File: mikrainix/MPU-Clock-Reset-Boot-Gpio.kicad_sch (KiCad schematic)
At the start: 17 parts, among them SW3 BPOR, SW4 BBOOT, U7 RV1106G3, Y2 32.768KHz, Y3 24MHz

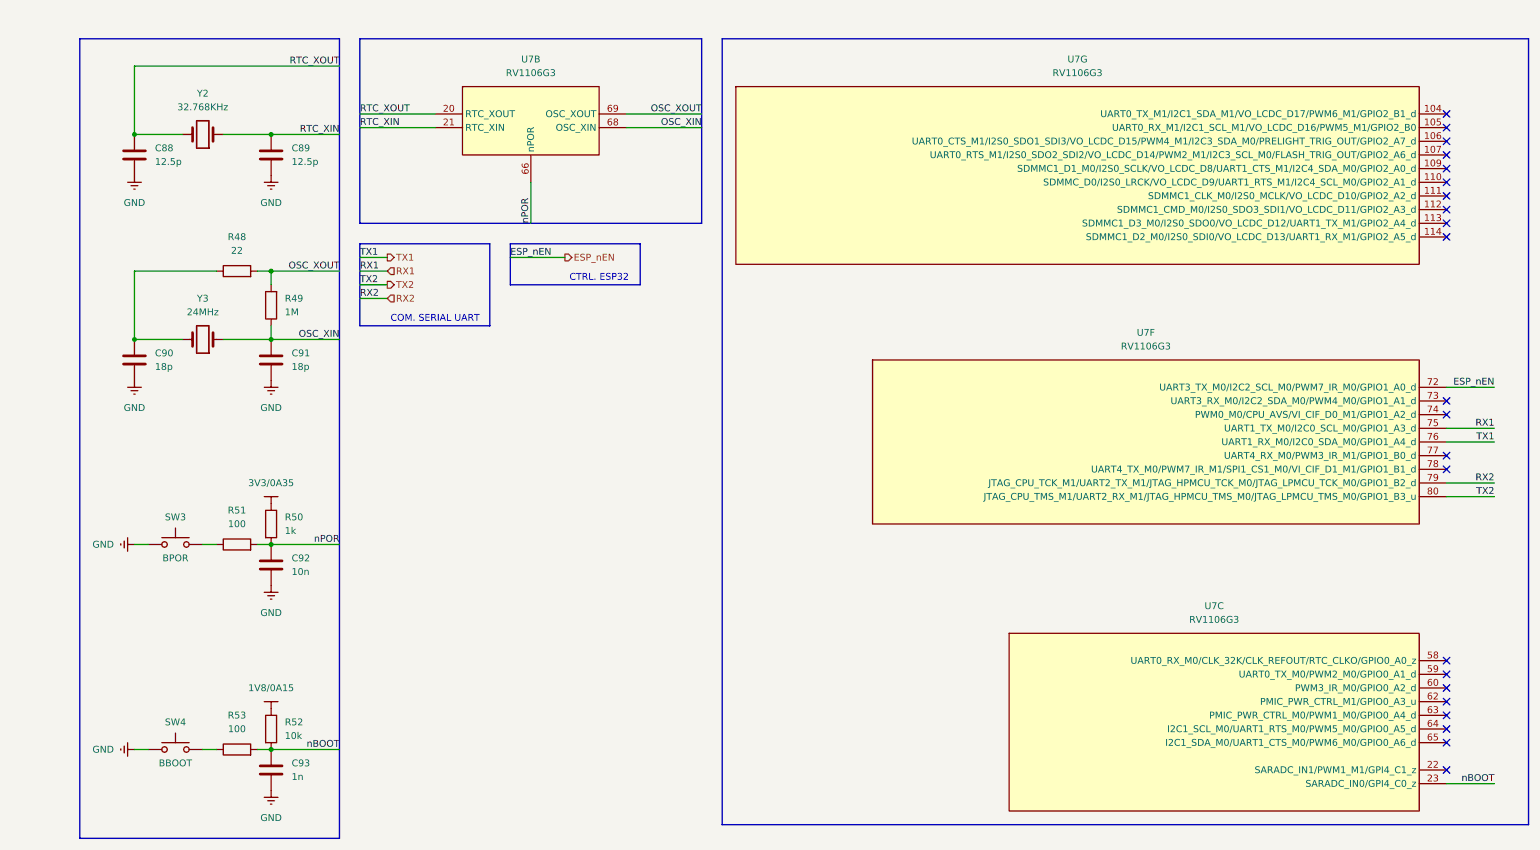
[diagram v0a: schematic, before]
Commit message: add MIS5001 camera and Ethernet, replace ESP32-C6-MINI > ESP32-MINI-1
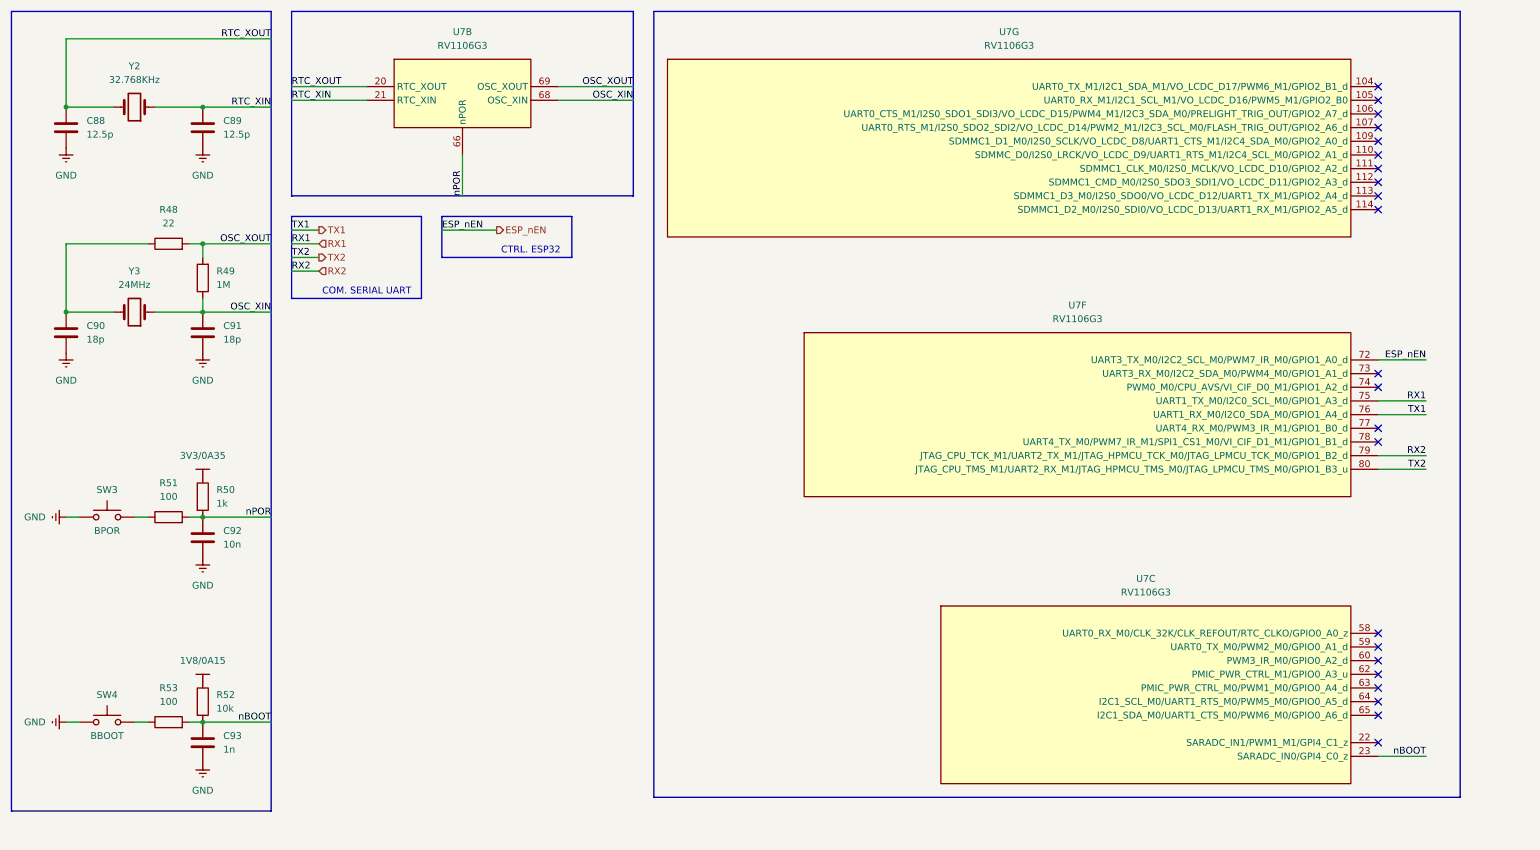
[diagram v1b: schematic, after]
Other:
- title: MPU – Clock, Reset, Boot & GPIO -> MPU–Clock, Reset, Boot & GPIO
- moved on the sheet: C88, C89, C90, C91, C92, C93, R48, R49, R50, R51, R52, R53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

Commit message: add microSD and resolve ERC issues
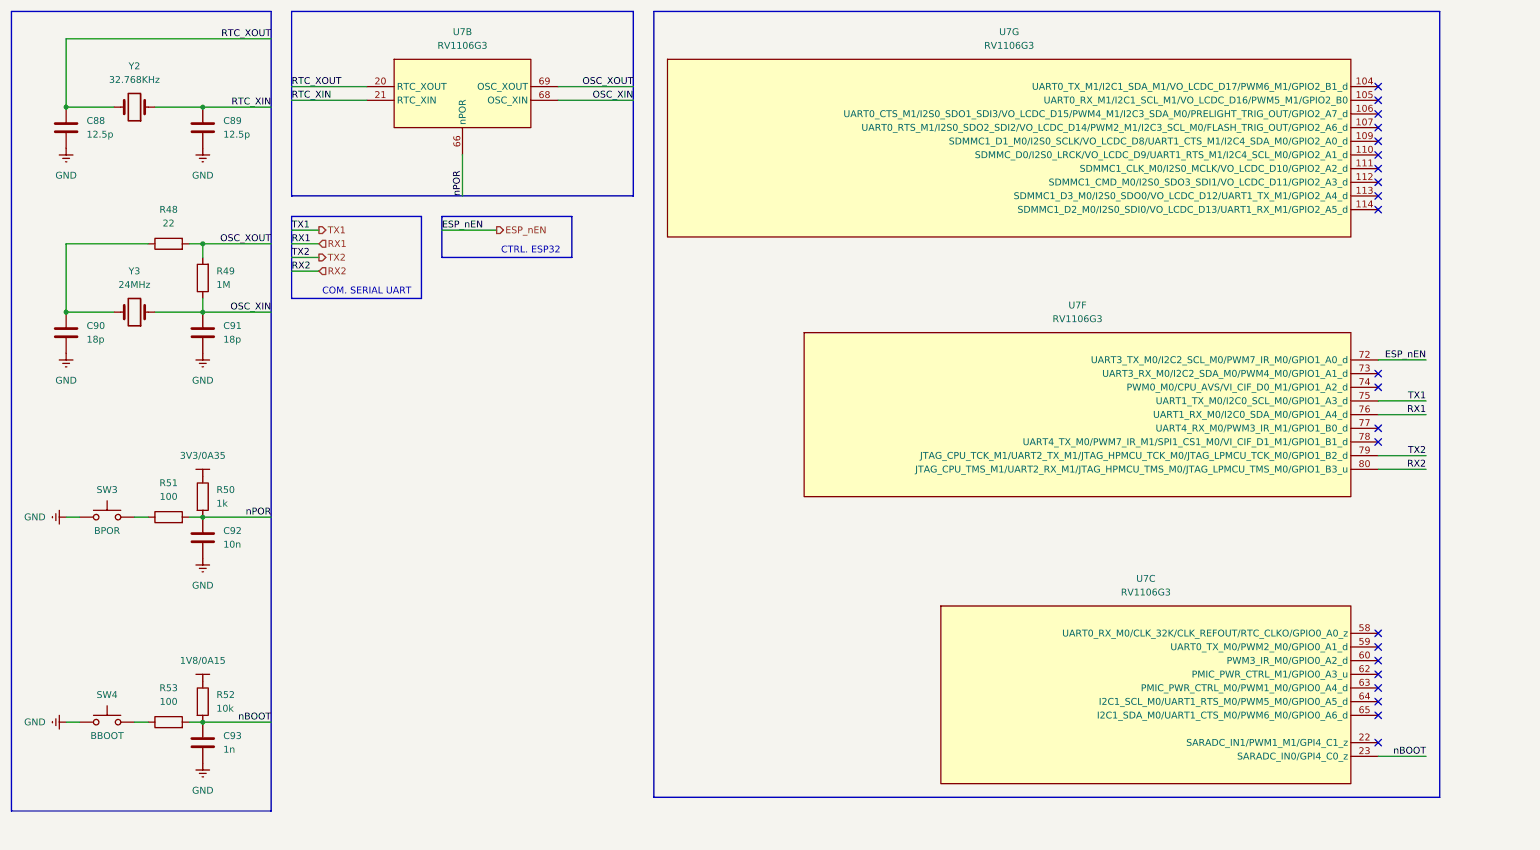
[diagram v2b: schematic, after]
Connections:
- net RX1: now also U7.76 (UART1_RX_M0/I2C0_SDA_M0/GPIO1_A4_d); no longer U7.75 (UART1_TX_M0/I2C0_SCL_M0/GPIO1_A3_d)
- net RX2: now also U7.80 (JTAG_CPU_TMS_M1/UART2_RX_M1/JTAG_HPMCU_TMS_M0/JTAG_LPMCU_TMS_M0/GPIO1_B3_u); no longer U7.79 (JTAG_CPU_TCK_M1/UART2_TX_M1/JTAG_HPMCU_TCK_M0/JTAG_LPMCU_TCK_M0/GPIO1_B2_d)
- net TX1: now also U7.75 (UART1_TX_M0/I2C0_SCL_M0/GPIO1_A3_d); no longer U7.76 (UART1_RX_M0/I2C0_SDA_M0/GPIO1_A4_d)
- net TX2: now also U7.79 (JTAG_CPU_TCK_M1/UART2_TX_M1/JTAG_HPMCU_TCK_M0/JTAG_LPMCU_TCK_M0/GPIO1_B2_d); no longer U7.80 (JTAG_CPU_TMS_M1/UART2_RX_M1/JTAG_HPMCU_TMS_M0/JTAG_LPMCU_TMS_M0/GPIO1_B3_u)
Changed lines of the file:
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@@
 	(title_block
 		(title "MPU–Clock, Reset, Boot & GPIO")
-		(date "2026-10-14")
+		(date "2026-10-21")
+		(rev "v0.1")
 		(comment 1 "Project repository: github.com/ndkimdavy/Mikrainix")
 		(comment 2 "Designed by: Kim Davy NDAYONGEJE")
@@
 	(rectangle
 		(start 134.62 15.24)
-		(end 284.48 161.29)
+		(end 280.67 161.29)
 		(stroke
 			(width 0.254)
@@
 	(wire
 		(pts
-			(xy 48.26 147.32) (xy 50.8 147.32)
+			(xy 269.24 100.33) (xy 278.13 100.33)
 		)
 		(stroke
@@
 	(wire
 		(pts
-			(xy 50.8 109.22) (xy 63.5 109.22)
+			(xy 48.26 147.32) (xy 50.8 147.32)
 		)
 		(stroke
@@
 	(wire
 		(pts
-			(xy 269.24 90.17) (xy 278.13 90.17)
+			(xy 50.8 109.22) (xy 63.5 109.22)
 		)
 		(stroke
@@
 	(wire
 		(pts
-			(xy 269.24 97.79) (xy 278.13 97.79)
+			(xy 72.39 55.88) (xy 67.31 55.88)
 		)
 		(stroke
@@
 	(wire
 		(pts
-			(xy 72.39 58.42) (xy 67.31 58.42)
+			(xy 25.4 71.12) (xy 34.29 71.12)
 		)
 		(stroke
@@
 	(wire
 		(pts
-			(xy 25.4 71.12) (xy 34.29 71.12)
+			(xy 269.24 97.79) (xy 278.13 97.79)
 		)
 		(stroke
@@
 	(wire
 		(pts
-			(xy 38.1 109.22) (xy 40.64 109.22)
+			(xy 269.24 87.63) (xy 278.13 87.63)
 		)
 		(stroke
@@
 	(wire
 		(pts
-			(xy 25.4 58.42) (xy 40.64 58.42)
+			(xy 38.1 109.22) (xy 40.64 109.22)
 		)
 		(stroke
@@
 	(wire
 		(pts
-			(xy 48.26 58.42) (xy 50.8 58.42)
+			(xy 25.4 58.42) (xy 40.64 58.42)
 		)
 		(stroke
@@
 	(wire
 		(pts
-			(xy 63.5 20.32) (xy 25.4 20.32)
+			(xy 269.24 90.17) (xy 278.13 90.17)
 		)
 		(stroke
@@
 	(wire
 		(pts
-			(xy 72.39 63.5) (xy 67.31 63.5)
+			(xy 72.39 58.42) (xy 67.31 58.42)
 		)
 		(stroke
@@
 	(wire
 		(pts
-			(xy 50.8 58.42) (xy 50.8 60.96)
+			(xy 48.26 58.42) (xy 50.8 58.42)
 		)
 		(stroke
@@
 	(wire
 		(pts
-			(xy 105.41 55.88) (xy 95.25 55.88)
+			(xy 63.5 20.32) (xy 25.4 20.32)
 		)
 		(stroke
@@
 	(wire
 		(pts
-			(xy 25.4 58.42) (xy 25.4 71.12)
+			(xy 50.8 58.42) (xy 50.8 60.96)
 		)
 		(stroke
@@
 	(wire
 		(pts
-			(xy 72.39 55.88) (xy 67.31 55.88)
+			(xy 105.41 55.88) (xy 95.25 55.88)
 		)
 		(stroke
@@
 	(wire
 		(pts
-			(xy 269.24 80.01) (xy 278.13 80.01)
+			(xy 25.4 58.42) (xy 25.4 71.12)
 		)
 		(stroke
@@
 	(wire
 		(pts
-			(xy 269.24 153.67) (xy 278.13 153.67)
+			(xy 72.39 63.5) (xy 67.31 63.5)
 		)
 		(stroke
@@
 	(wire
 		(pts
-			(xy 116.84 31.75) (xy 130.81 31.75)
+			(xy 269.24 80.01) (xy 278.13 80.01)
 		)
 		(stroke
@@
 	(wire
 		(pts
-			(xy 67.31 31.75) (xy 81.28 31.75)
+			(xy 269.24 153.67) (xy 278.13 153.67)
 		)
 		(stroke
@@
 	(wire
 		(pts
-			(xy 269.24 100.33) (xy 278.13 100.33)
+			(xy 116.84 31.75) (xy 130.81 31.75)
 		)
 		(stroke
@@
 	(wire
 		(pts
-			(xy 99.06 41.91) (xy 99.06 49.53)
+			(xy 67.31 31.75) (xy 81.28 31.75)
 		)
 		(stroke
@@
 	(wire
 		(pts
-			(xy 50.8 33.02) (xy 63.5 33.02)
+			(xy 99.06 41.91) (xy 99.06 49.53)
 		)
 		(stroke
@@
 	(wire
 		(pts
-			(xy 50.8 71.12) (xy 63.5 71.12)
+			(xy 50.8 33.02) (xy 63.5 33.02)
 		)
 		(stroke
@@
 	(wire
 		(pts
-			(xy 269.24 87.63) (xy 278.13 87.63)
+			(xy 50.8 71.12) (xy 63.5 71.12)
 		)
 		(stroke
@@
 		)
 	)
-	(label "nPOR"
-		(at 99.06 49.53 90)
+	(label "TX2"
+		(at 67.31 60.96 0)
 		(effects
 			(font
@@
 		)
 	)
-	(label "nBOOT"
-		(at 278.13 153.67 180)
+	(label "nPOR"
+		(at 99.06 49.53 90)
 		(effects
 			(font
 				(size 1.27 1.27)
 			)
-			(justify right bottom)
+			(justify left bottom)
 		)
 	)
-	(label "TX2"
-		(at 67.31 60.96 0)
+	(label "nBOOT"
+		(at 278.13 153.67 180)
 		(effects
 			(font
 				(size 1.27 1.27)
 			)
-			(justify left bottom)
+			(justify right bottom)
 		)
 	)
 	(label "RX2"
-		(at 278.13 97.79 180)
+		(at 278.13 100.33 180)
 		(effects
 			(font
@@
 		)
 	)
-	(label "RX2"
-		(at 67.31 63.5 0)
-		(effects
-			(font
-				(size 1.27 1.27)
-			)
-			(justify left bottom)
-		)
-	)
 	(label "TX1"
-		(at 278.13 90.17 180)
+		(at 278.13 87.63 180)
 		(effects
 			(font
@@
 	)
 	(label "TX2"
-		(at 278.13 100.33 180)
+		(at 278.13 97.79 180)
 		(effects
 			(font
@@
 		)
 	)
+	(label "TX1"
+		(at 67.31 55.88 0)
+		(effects
+			(font
+				(size 1.27 1.27)
+			)
+			(justify left bottom)
+		)
+	)
 	(label "nPOR"
 		(at 63.5 109.22 180)
@@
 	)
 	(label "RX1"
-		(at 278.13 87.63 180)
+		(at 278.13 90.17 180)
 		(effects
 			(font
@@
 		)
 	)
-	(label "TX1"
-		(at 67.31 55.88 0)
+	(label "RTC_XIN"
+		(at 63.5 33.02 180)
 		(effects
 			(font
 				(size 1.27 1.27)
 			)
-			(justify left bottom)
+			(justify right bottom)
 		)
 	)
-	(label "RTC_XIN"
-		(at 63.5 33.02 180)
+	(label "ESP_nEN"
+		(at 278.13 80.01 180)
 		(effects
 			(font
@@
 		)
 	)
-	(label "ESP_nEN"
-		(at 278.13 80.01 180)
+	(label "RX2"
+		(at 67.31 63.5 0)
 		(effects
 			(font
 				(size 1.27 1.27)
 			)
-			(justify right bottom)
+			(justify left bottom)
 		)
 	)
@@
 		)
 	)
-	(hierarchical_label "ESP_nEN"
+	(hierarchical_label "TX2"
 		(shape output)
-		(at 105.41 55.88 0)
+		(at 72.39 60.96 0)
 		(effects
 			(font
@@
 		)
 	)
-	(hierarchical_label "RX1"
-		(shape input)
-		(at 72.39 58.42 0)
+	(hierarchical_label "ESP_nEN"
+		(shape output)
+		(at 105.41 55.88 0)
 		(effects
 			(font
@@
 		)
 	)
-	(hierarchical_label "TX2"
-		(shape output)
-		(at 72.39 60.96 0)
+	(hierarchical_label "RX1"
+		(shape input)
+		(at 72.39 58.42 0)
 		(effects
 			(font
@@
 		(dnp no)
 		(fields_autoplaced yes)
-		(property "Reference" "#PWR0130"
+		(property "Reference" "#PWR0135"
 			(at 50.8 85.09 0)
 			(hide yes)
@@
 			(project "mikrainix"
 				(path "/19082ed6-8f17-4d62-ab42-418ea03b55ea/a833726d-e6a4-4dfb-afe7-f82d945434d0"
-					(reference "#PWR0130")
+					(reference "#PWR0135")
 					(unit 1)
 				)
@@
 		(dnp no)
 		(fields_autoplaced yes)
-		(property "Reference" "#PWR0135"
+		(property "Reference" "#PWR0140"
 			(at 19.05 147.32 0)
 			(hide yes)
@@
 			(project "mikrainix"
 				(path "/19082ed6-8f17-4d62-ab42-418ea03b55ea/a833726d-e6a4-4dfb-afe7-f82d945434d0"
-					(reference "#PWR0135")
+					(reference "#PWR0140")
 					(unit 1)
 				)
@@
 		(dnp no)
 		(fields_autoplaced yes)
-		(property "Reference" "#PWR0127"
+		(property "Reference" "#PWR0132"
 			(at 25.4 46.99 0)
 			(hide yes)
@@
 			(project "mikrainix"
 				(path "/19082ed6-8f17-4d62-ab42-418ea03b55ea/a833726d-e6a4-4dfb-afe7-f82d945434d0"
-					(reference "#PWR0127")
+					(reference "#PWR0132")
 					(unit 1)
 				)
@@
 		(dnp no)
 		(fields_autoplaced yes)
-		(property "Reference" "#PWR0134"
+		(property "Reference" "#PWR0139"
 			(at 50.8 144.78 0)
 			(hide yes)
@@
 			(project "mikrainix"
 				(path "/19082ed6-8f17-4d62-ab42-418ea03b55ea/a833726d-e6a4-4dfb-afe7-f82d945434d0"
-					(reference "#PWR0134")
+					(reference "#PWR0139")
 					(unit 1)
 				)
@@
 		(dnp no)
 		(fields_autoplaced yes)
-		(property "Reference" "#PWR0129"
+		(property "Reference" "#PWR0134"
 			(at 25.4 85.09 0)
 			(hide yes)
@@
 			(project "mikrainix"
 				(path "/19082ed6-8f17-4d62-ab42-418ea03b55ea/a833726d-e6a4-4dfb-afe7-f82d945434d0"
-					(reference "#PWR0129")
+					(reference "#PWR0134")
 					(unit 1)
 				)
@@
 		(dnp no)
 		(fields_autoplaced yes)
-		(property "Reference" "#PWR0128"
+		(property "Reference" "#PWR0133"
 			(at 50.8 46.99 0)
 			(hide yes)
@@
 			(project "mikrainix"
 				(path "/19082ed6-8f17-4d62-ab42-418ea03b55ea/a833726d-e6a4-4dfb-afe7-f82d945434d0"
-					(reference "#PWR0128")
+					(reference "#PWR0133")
 					(unit 1)
 				)
@@
 		(dnp no)
 		(fields_autoplaced yes)
-		(property "Reference" "#PWR0132"
+		(property "Reference" "#PWR0137"
 			(at 19.05 109.22 0)
 			(hide yes)
@@
 			(project "mikrainix"
 				(path "/19082ed6-8f17-4d62-ab42-418ea03b55ea/a833726d-e6a4-4dfb-afe7-f82d945434d0"
-					(reference "#PWR0132")
+					(reference "#PWR0137")
 					(unit 1)
 				)
@@
 		(dnp no)
 		(fields_autoplaced yes)
-		(property "Reference" "#PWR0133"
+		(property "Reference" "#PWR0138"
 			(at 50.8 123.19 0)
 			(hide yes)
@@
 			(project "mikrainix"
 				(path "/19082ed6-8f17-4d62-ab42-418ea03b55ea/a833726d-e6a4-4dfb-afe7-f82d945434d0"
-					(reference "#PWR0133")
+					(reference "#PWR0138")
 					(unit 1)
 				)
@@
 		(dnp no)
 		(fields_autoplaced yes)
-		(property "Reference" "#PWR0131"
+		(property "Reference" "#PWR0136"
 			(at 50.8 106.68 0)
 			(hide yes)
@@
 			(project "mikrainix"
 				(path "/19082ed6-8f17-4d62-ab42-418ea03b55ea/a833726d-e6a4-4dfb-afe7-f82d945434d0"
-					(reference "#PWR0131")
+					(reference "#PWR0136")
 					(unit 1)
 				)
@@
 		(dnp no)
 		(fields_autoplaced yes)
-		(property "Reference" "#PWR0136"
+		(property "Reference" "#PWR0141"
 			(at 50.8 161.29 0)
 			(hide yes)
@@
 			(project "mikrainix"
 				(path "/19082ed6-8f17-4d62-ab42-418ea03b55ea/a833726d-e6a4-4dfb-afe7-f82d945434d0"
-					(reference "#PWR0136")
+					(reference "#PWR0141")
 					(unit 1)
 				)

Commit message: add ESD protection
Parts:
- removed U7: RV1106G3, mikrainix-RV1106G3:QFN35P1230X1230X90-129N, symbol mikrainix-RV1106G3:RV1106G3
- added U8: RV1106G3, mikrainix-RV1106G3:QFN35P1230X1230X90-129N, symbol mikrainix-RV1106G3:RV1106G3
- renumbered C90 to C89, C89 to C90, R51 to R49, R53 to R50, R49 to R51, R50 to R52, R52 to R53
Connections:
- net ESP_nEN: now also U8.72 (UART3_TX_M0/I2C2_SCL_M0/PWM7_IR_M0/GPIO1_A0_d)
- net OSC_XIN: now also U8.68 (OSC_XIN)
- net OSC_XOUT: now also U8.69 (OSC_XOUT)
- net RTC_XIN: now also U8.21 (RTC_XIN)
- net RTC_XOUT: now also U8.20 (RTC_XOUT)
- net RX1: now also U8.76 (UART1_RX_M0/I2C0_SDA_M0/GPIO1_A4_d)
- net RX2: now also U8.80 (JTAG_CPU_TMS_M1/UART2_RX_M1/JTAG_HPMCU_TMS_M0/JTAG_LPMCU_TMS_M0/GPIO1_B3_u)
- net TX1: now also U8.75 (UART1_TX_M0/I2C0_SCL_M0/GPIO1_A3_d)
- net TX2: now also U8.79 (JTAG_CPU_TCK_M1/UART2_TX_M1/JTAG_HPMCU_TCK_M0/JTAG_LPMCU_TCK_M0/GPIO1_B2_d)
- net nBOOT: now also U8.23 (SARADC_IN0/GPI4_C0_z)
- net nPOR: now also U8.66 (nPOR)
